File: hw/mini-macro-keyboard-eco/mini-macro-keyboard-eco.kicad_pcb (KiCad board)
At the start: 2 copper layers, 32 parts, among them J0 USB, J1 DEBUG_SWD, SW1 SW_Cherry_MX_1.00u_PCB, SW2 SW_Cherry_MX_1.00u_PCB, SW3 SW_Cherry_MX_1.00u_PCB, SW5 LAYOUT, SW6 BACKLIGHT, U1 USBLC6-2SC6, U2 XC6206P322MR, U3 STM32F070F6P6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

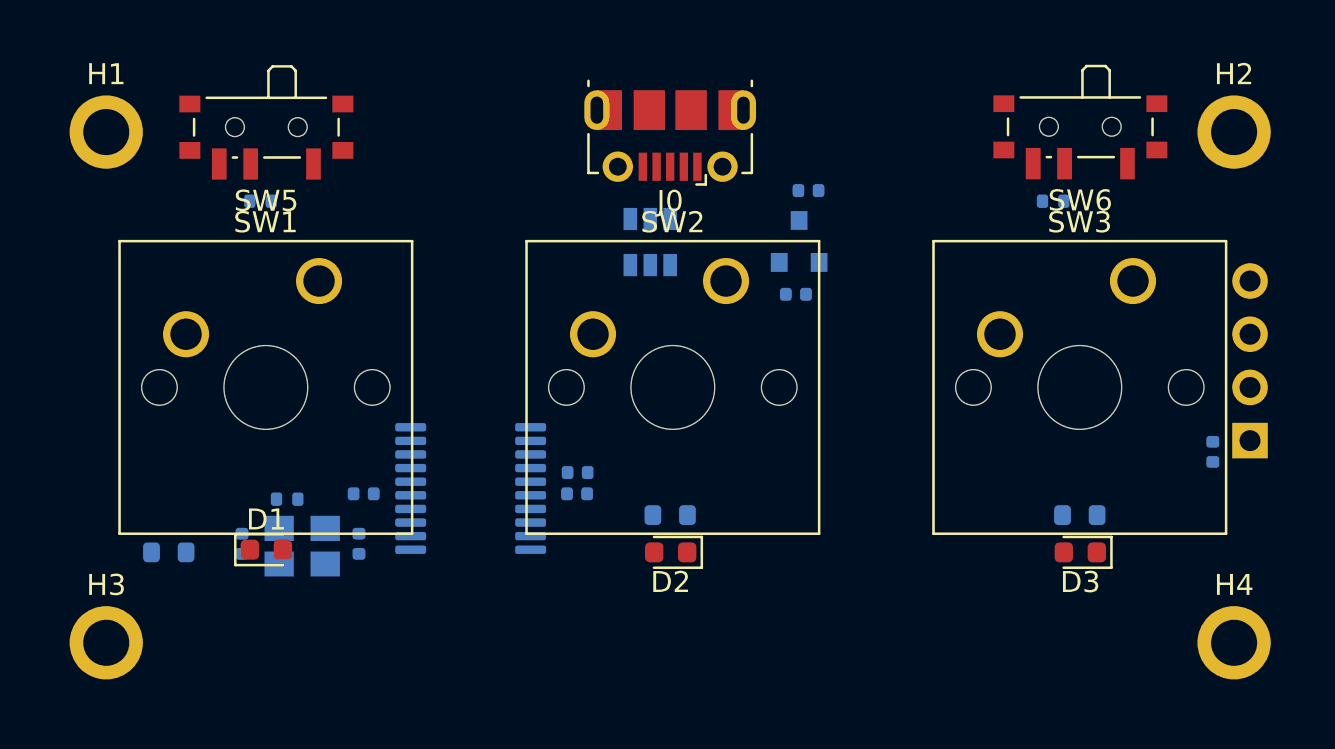
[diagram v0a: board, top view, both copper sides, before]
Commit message: feat(hw): improve layout
Signed-off-by: Ivan Kovalenko <s1ckretbox@gmail.com>
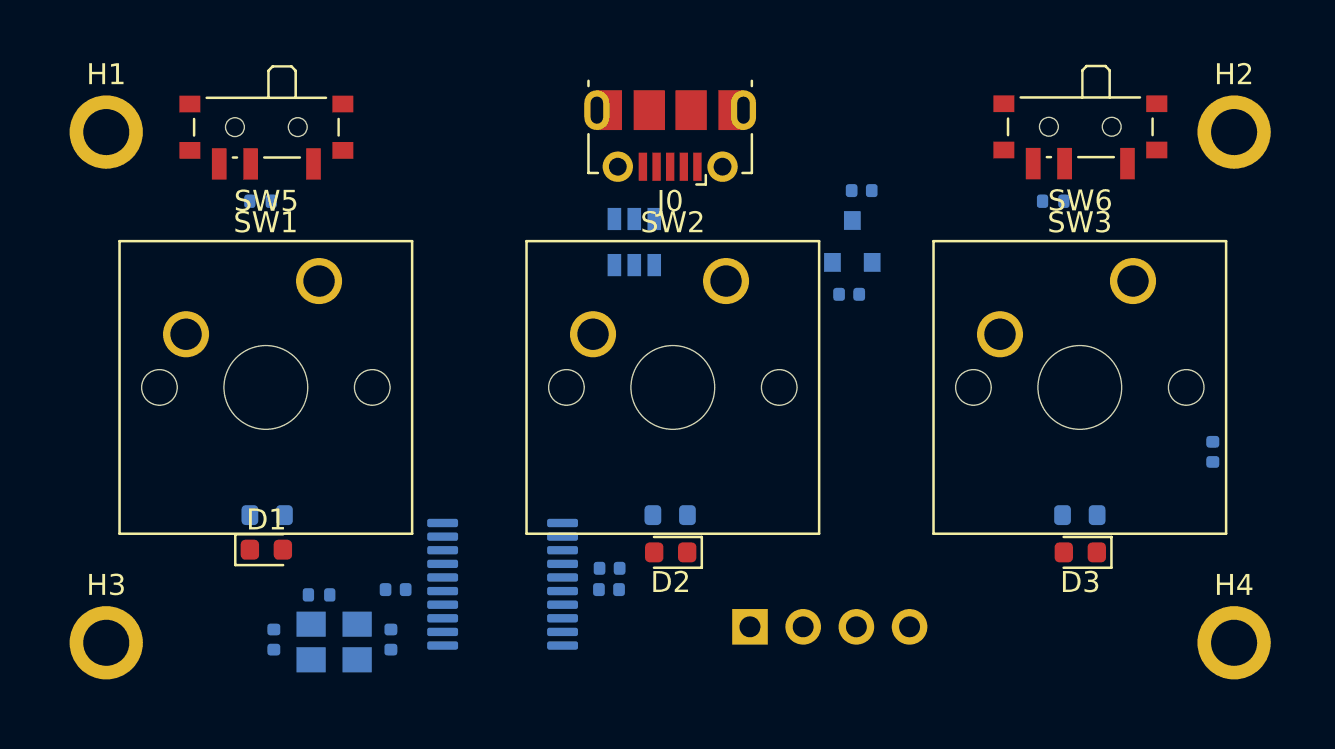
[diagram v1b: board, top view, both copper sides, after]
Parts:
- moved J1 25.5 mm to (147.1, 111.8), turned to 270 degrees
- moved R1 5.02 mm to (124.0, 106.4), turned to 0 degrees
- moved C0 4.82 mm to (129.9, 112.4)
- moved C1 4.82 mm to (124.3, 112.4)
- moved C2 4.82 mm to (140.3, 110.0)
- moved C3 4.82 mm to (130.1, 110.0)
- moved R0 4.82 mm to (126.5, 110.2)
- moved Y1 4.82 mm to (127.2, 112.5)
- moved C4 4.82 mm to (140.4, 109.0)
- moved U3 4.82 mm to (135.3, 109.7)
- moved C5 2.54 mm to (152.4, 90.9)
- moved C6 2.54 mm to (151.8, 95.9)
- moved U2 2.54 mm to (152.0, 93.4)
- moved U1 0.76 mm to (141.5, 93.4)
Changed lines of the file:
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@@
   )
   (module Capacitor_SMD:C_0402_1005Metric (layer B.Cu)
-    (at 138.811 105.41)
+    (at 140.335 109.982)
     (descr "Capacitor SMD 0402 (1005 Metric), square (rectangular) end terminal, IPC_7351 nominal, (Body size source: IPC-SM-782 page 76, https://www.pcb-3d.com/wordpress/wp-content/uploads/ipc-sm-782a_amendment_1_and_2.pdf), generated with kicad-footprint-generator")
     (tags capacitor)
@@
   )
   (module Capacitor_SMD:C_0402_1005Metric (layer B.Cu)
-    (at 128.623 105.41 180)
+    (at 130.147 109.982 180)
     (descr "Capacitor SMD 0402 (1005 Metric), square (rectangular) end terminal, IPC_7351 nominal, (Body size source: IPC-SM-782 page 76, https://www.pcb-3d.com/wordpress/wp-content/uploads/ipc-sm-782a_amendment_1_and_2.pdf), generated with kicad-footprint-generator")
     (tags capacitor)
@@
   )
   (module Capacitor_SMD:C_0402_1005Metric (layer B.Cu)
-    (at 138.839 104.394)
+    (at 140.363 108.966)
     (descr "Capacitor SMD 0402 (1005 Metric), square (rectangular) end terminal, IPC_7351 nominal, (Body size source: IPC-SM-782 page 76, https://www.pcb-3d.com/wordpress/wp-content/uploads/ipc-sm-782a_amendment_1_and_2.pdf), generated with kicad-footprint-generator")
     (tags capacitor)
@@
   )
   (module Capacitor_SMD:C_0402_1005Metric (layer B.Cu)
-    (at 122.809 107.795 90)
+    (at 124.333 112.367 90)
     (descr "Capacitor SMD 0402 (1005 Metric), square (rectangular) end terminal, IPC_7351 nominal, (Body size source: IPC-SM-782 page 76, https://www.pcb-3d.com/wordpress/wp-content/uploads/ipc-sm-782a_amendment_1_and_2.pdf), generated with kicad-footprint-generator")
     (tags capacitor)
@@
   )
   (module Capacitor_SMD:C_0402_1005Metric (layer B.Cu)
-    (at 128.397 107.795 270)
+    (at 129.921 112.367 270)
     (descr "Capacitor SMD 0402 (1005 Metric), square (rectangular) end terminal, IPC_7351 nominal, (Body size source: IPC-SM-782 page 76, https://www.pcb-3d.com/wordpress/wp-content/uploads/ipc-sm-782a_amendment_1_and_2.pdf), generated with kicad-footprint-generator")
     (tags capacitor)
@@
   )
   (module Capacitor_SMD:C_0402_1005Metric (layer B.Cu)
-    (at 149.86 90.932)
+    (at 152.4 90.932)
     (descr "Capacitor SMD 0402 (1005 Metric), square (rectangular) end terminal, IPC_7351 nominal, (Body size source: IPC-SM-782 page 76, https://www.pcb-3d.com/wordpress/wp-content/uploads/ipc-sm-782a_amendment_1_and_2.pdf), generated with kicad-footprint-generator")
     (tags capacitor)
@@
   )
   (module Capacitor_SMD:C_0402_1005Metric (layer B.Cu)
-    (at 149.2605 95.885)
+    (at 151.8005 95.885)
     (descr "Capacitor SMD 0402 (1005 Metric), square (rectangular) end terminal, IPC_7351 nominal, (Body size source: IPC-SM-782 page 76, https://www.pcb-3d.com/wordpress/wp-content/uploads/ipc-sm-782a_amendment_1_and_2.pdf), generated with kicad-footprint-generator")
     (tags capacitor)
@@
   )
   (module Connector_PinHeader_2.54mm:PinHeader_1x04_P2.54mm_Horizontal (layer B.Cu)
-    (at 170.942 102.87)
+    (at 147.066 111.76 270)
     (descr "Through hole angled pin header, 1x04, 2.54mm pitch, 6mm pin length, single row")
     (tags "Through hole angled pin header THT 1x04 2.54mm single row")
-    (fp_text reference J1 (at 4.385 2.27) (layer B.SilkS)
-      (effects (font (size 1 1) (thickness 0.15)) (justify mirror))
-    )
-    (fp_text value DEBUG_SWD (at 4.385 -9.89) (layer B.Fab)
+    (fp_text reference J1 (at 4.385 2.27 90) (layer B.SilkS)
+      (effects (font (size 1 1) (thickness 0.15)) (justify mirror))
+    )
+    (fp_text value DEBUG_SWD (at 4.385 -9.89 90) (layer B.Fab)
       (effects (font (size 1 1) (thickness 0.15)) (justify mirror))
     )
@@
     (fp_line (start 4.04 1.27) (end 4.04 -8.89) (layer B.Fab) (width 0.1))
     (fp_line (start 2.135 1.27) (end 4.04 1.27) (layer B.Fab) (width 0.1))
-    (fp_text user %R (at 2.77 -3.81 -90) (layer B.Fab)
-      (effects (font (size 1 1) (thickness 0.15)) (justify mirror))
-    )
-    (pad 1 thru_hole rect (at 0 0) (size 1.7 1.7) (drill 1) (layers *.Cu *.Mask)
+    (fp_text user %R (at 2.77 -3.81 180) (layer B.Fab)
+      (effects (font (size 1 1) (thickness 0.15)) (justify mirror))
+    )
+    (pad 1 thru_hole rect (at 0 0 270) (size 1.7 1.7) (drill 1) (layers *.Cu *.Mask)
       (net 2 +3V3))
-    (pad 2 thru_hole oval (at 0 -2.54) (size 1.7 1.7) (drill 1) (layers *.Cu *.Mask)
+    (pad 2 thru_hole oval (at 0 -2.54 270) (size 1.7 1.7) (drill 1) (layers *.Cu *.Mask)
       (net 17 SWDIO))
-    (pad 3 thru_hole oval (at 0 -5.08) (size 1.7 1.7) (drill 1) (layers *.Cu *.Mask)
+    (pad 3 thru_hole oval (at 0 -5.08 270) (size 1.7 1.7) (drill 1) (layers *.Cu *.Mask)
       (net 18 SWCLK))
-    (pad 4 thru_hole oval (at 0 -7.62) (size 1.7 1.7) (drill 1) (layers *.Cu *.Mask)
+    (pad 4 thru_hole oval (at 0 -7.62 270) (size 1.7 1.7) (drill 1) (layers *.Cu *.Mask)
       (net 1 GND))
     (model ${KISYS3DMOD}/Connector_PinHeader_2.54mm.3dshapes/PinHeader_1x04_P2.54mm_Horizontal.wrl
@@
   )
   (module Resistor_SMD:R_0402_1005Metric (layer B.Cu)
-    (at 124.97 105.664 180)
+    (at 126.494 110.236 180)
     (descr "Resistor SMD 0402 (1005 Metric), square (rectangular) end terminal, IPC_7351 nominal, (Body size source: IPC-SM-782 page 72, https://www.pcb-3d.com/wordpress/wp-content/uploads/ipc-sm-782a_amendment_1_and_2.pdf), generated with kicad-footprint-generator")
     (tags resistor)
@@
   )
   (module Resistor_SMD:R_0603_1608Metric (layer B.Cu)
-    (at 119.317 108.204 180)
+    (at 124.015 106.426)
     (descr "Resistor SMD 0603 (1608 Metric), square (rectangular) end terminal, IPC_7351 nominal, (Body size source: IPC-SM-782 page 72, https://www.pcb-3d.com/wordpress/wp-content/uploads/ipc-sm-782a_amendment_1_and_2.pdf), generated with kicad-footprint-generator")
     (tags resistor)
@@
       (effects (font (size 0.4 0.4) (thickness 0.06)) (justify mirror))
     )
-    (pad 1 smd roundrect (at -0.825 0 180) (size 0.8 0.95) (layers B.Cu B.Paste B.Mask) (roundrect_rratio 0.25)
+    (pad 1 smd roundrect (at -0.825 0) (size 0.8 0.95) (layers B.Cu B.Paste B.Mask) (roundrect_rratio 0.25)
       (net 8 "Net-(D1-Pad1)"))
-    (pad 2 smd roundrect (at 0.825 0 180) (size 0.8 0.95) (layers B.Cu B.Paste B.Mask) (roundrect_rratio 0.25)
+    (pad 2 smd roundrect (at 0.825 0) (size 0.8 0.95) (layers B.Cu B.Paste B.Mask) (roundrect_rratio 0.25)
       (net 1 GND))
     (model ${KISYS3DMOD}/Resistor_SMD.3dshapes/R_0603_1608Metric.wrl
@@
   )
   (module Package_TO_SOT_SMD:SOT-23-6 (layer B.Cu)
-    (at 142.306 93.388 90)
+    (at 141.544 93.388 90)
     (descr "6-pin SOT-23 package")
     (tags SOT-23-6)
@@
   )
   (module Package_TO_SOT_SMD:SOT-23 (layer B.Cu)
-    (at 149.413 93.361 90)
+    (at 151.953 93.361 90)
     (descr "SOT-23, Standard")
     (tags SOT-23)
@@
   )
   (module Package_SO:TSSOP-20_4.4x6.5mm_P0.65mm (layer B.Cu)
-    (at 133.731 105.156)
+    (at 135.255 109.728)
     (descr "TSSOP, 20 Pin (JEDEC MO-153 Var AC https://www.jedec.org/document_search?search_api_views_fulltext=MO-153), generated with kicad-footprint-generator ipc_gullwing_generator.py")
     (tags "TSSOP SO")
@@
   )
   (module Crystal:Crystal_SMD_3225-4Pin_3.2x2.5mm (layer B.Cu)
-    (at 125.687 107.911 180)
+    (at 127.211 112.483 180)
     (descr "SMD Crystal SERIES SMD3225/4 http://www.txccrystal.com/images/pdf/7m-accuracy.pdf, 3.2x2.5mm^2 package")
     (tags "SMD SMT crystal")

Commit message: feat(hw): add edges
Signed-off-by: Ivan Kovalenko <s1ckretbox@gmail.com>
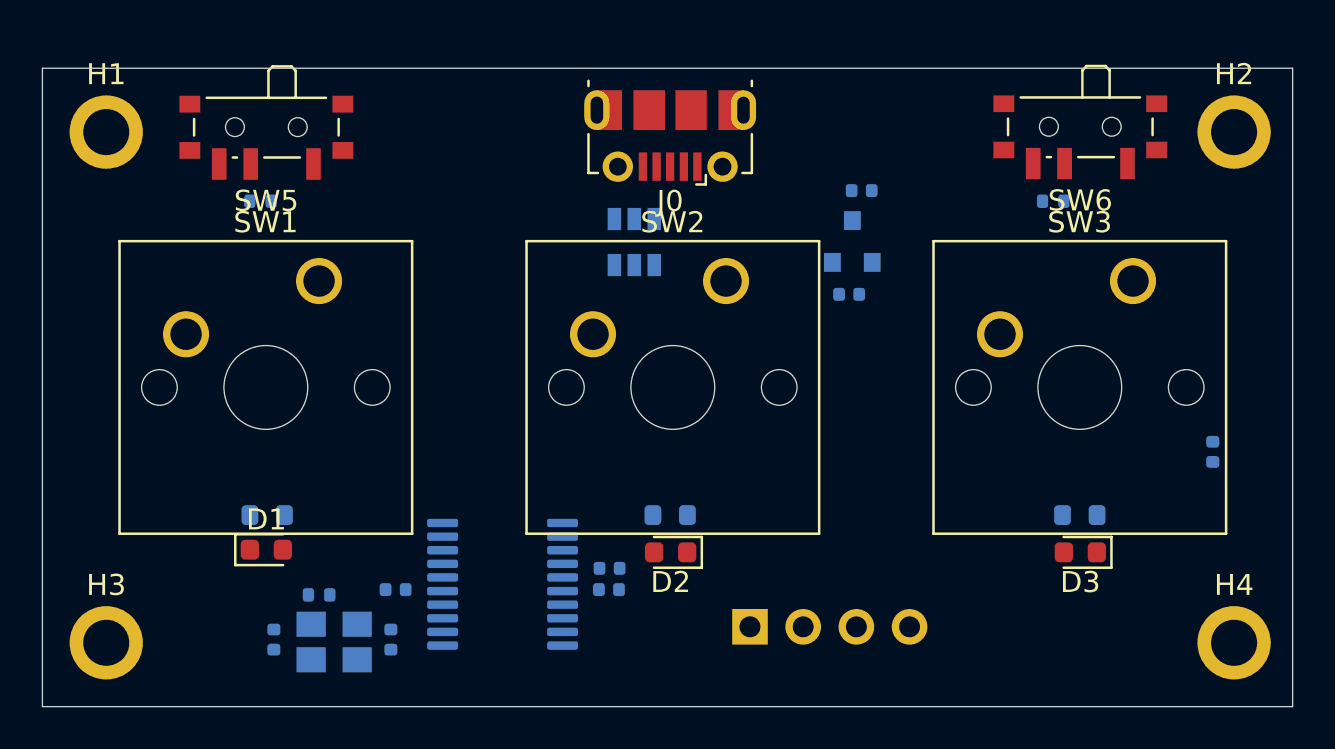
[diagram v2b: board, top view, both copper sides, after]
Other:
- board outline added: 59.7 x 30.5 mm
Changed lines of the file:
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@@
   (general
     (thickness 1.6)
-    (drawings 0)
+    (drawings 6)
     (tracks 0)
     (zones 0)
@@
     )
   )
+  (gr_line (start 113.284 85.09) (end 116.332 85.09) (layer Edge.Cuts) (width 0.05))
+  (gr_line (start 113.284 115.57) (end 113.284 85.09) (layer Edge.Cuts) (width 0.05))
+  (gr_line (start 172.974 115.57) (end 113.284 115.57) (layer Edge.Cuts) (width 0.05))
+  (gr_line (start 172.974 85.09) (end 172.974 115.57) (layer Edge.Cuts) (width 0.05))
+  (gr_line (start 170.18 85.09) (end 172.974 85.09) (layer Edge.Cuts) (width 0.05))
+  (gr_line (start 116.332 85.09) (end 170.18 85.09) (layer Edge.Cuts) (width 0.05))
 )

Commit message: feat(hw): move usb-b to the back layer
Signed-off-by: Ivan Kovalenko <s1ckretbox@gmail.com>
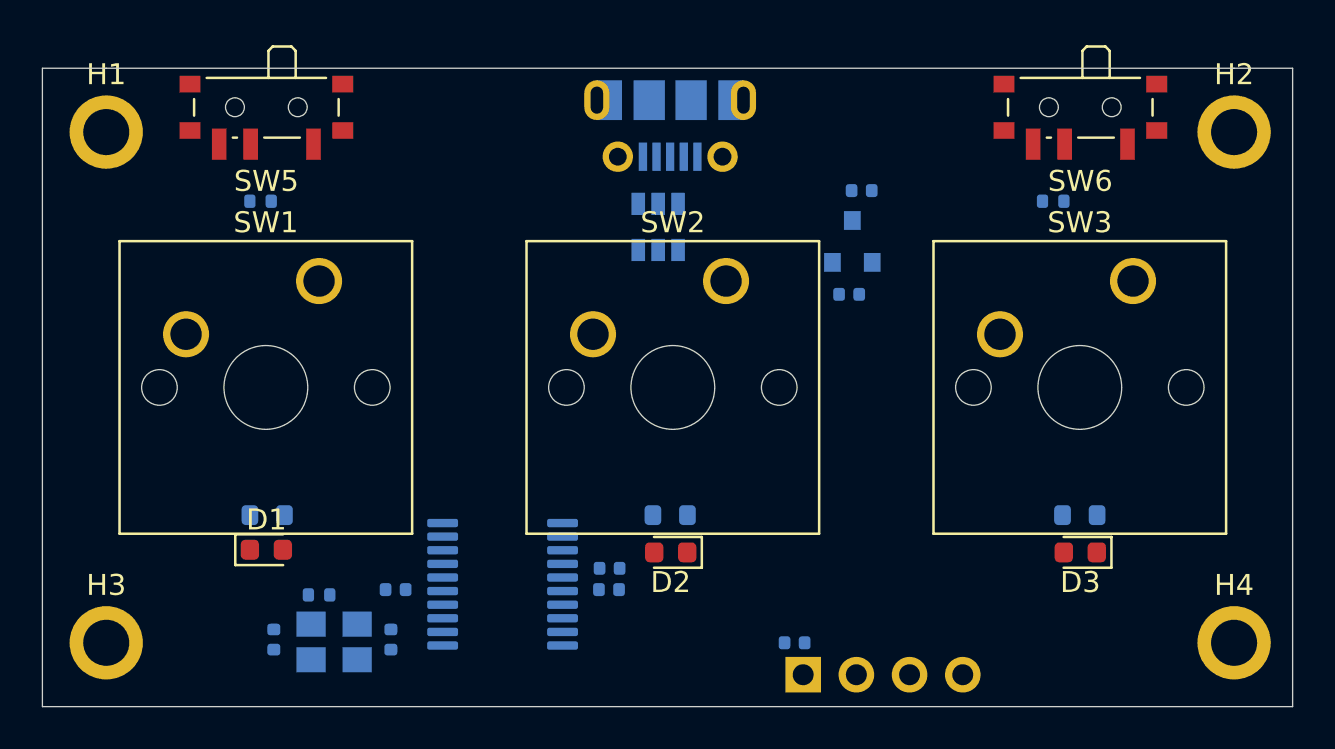
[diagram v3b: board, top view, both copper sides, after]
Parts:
- J0: moved to B.Cu
- moved C7 21.9 mm to (149.2, 112.5), turned to 180 degrees
- moved J1 3.42 mm to (149.6, 114.0)
- moved U1 1.35 mm to (142.7, 92.7), turned to 270 degrees
- moved SW5 0.95 mm to (124.0, 87.3)
- moved SW6 0.93 mm to (162.8, 87.3)
- moved J0 0.48 mm to (143.3, 87.9), turned to 0 degrees

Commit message: feat(hw): add rooting
Signed-off-by: Ivan Kovalenko <s1ckretbox@gmail.com>
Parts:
- moved R5 39.2 mm to (162.9, 91.5), turned to 0 degrees
- moved SW6 39.0 mm to (123.8, 87.1)
- moved SW5 39.0 mm to (162.9, 87.1)
- moved R6 36.8 mm to (124.8, 91.6), turned to 180 degrees
- moved C7 2.60 mm to (146.6, 112.9)
- moved R0 1.48 mm to (127.9, 110.7)
- moved R3 1.33 mm to (162.8, 105.1)
- moved R2 1.33 mm to (143.3, 105.1)
- moved R1 1.33 mm to (124.0, 105.1)
- moved J1 1.14 mm to (149.6, 112.9)
- moved U1 0.93 mm to (142.6, 93.6)
- moved C0 0.52 mm to (130.0, 112.9)
- moved C1 0.52 mm to (124.5, 112.9)
- moved Y1 0.52 mm to (127.3, 113.0)
- moved H1 0.51 mm to (116.8, 88.1)
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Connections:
- U1 pad 1: USB_CONN_D+ -> USB_CONN_D-
- U1 pad 3: USB_CONN_D- -> USB_CONN_D+
- U1 pad 4: USB_D- -> USB_D+
- U1 pad 6: USB_D+ -> USB_D-
- U3 pad 11: SW_1 -> SW_3
- U3 pad 13: SW_3 -> SW_1
- U3 pad 6: LED_1 -> LED_3
- U3 pad 9: LED_3 -> LED_1
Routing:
- net SW_LAYOUT: track 0.00 -> 39.1 mm, vias 0 -> 2
- net GND: track 0.00 -> 30.6 mm, vias 0 -> 10
- net LED_3: track 0.00 -> 30.2 mm, vias 0 -> 1
- net SW_1: track 0.00 -> 26.0 mm, vias 0 -> 1
- net SW_3: track 0.00 -> 25.2 mm, vias 0 -> 1
- net +5V: track 0.00 -> 23.1 mm, vias 0 -> 3
- net USB_D+: track 0.00 -> 22.9 mm
- net USB_D-: track 0.00 -> 22.1 mm
- net SW_BACKLIGHT: track 0.00 -> 20.1 mm
- net +3V3: track 0.00 -> 18.2 mm, vias 0 -> 4
- net SWCLK: track 0.00 -> 17.7 mm
- net SWDIO: track 0.00 -> 15.5 mm
- net SW_2: track 0.00 -> 13.2 mm, vias 0 -> 1
- net LED_2: track 0.00 -> 10.3 mm, vias 0 -> 1
- net LED_1: track 0.00 -> 8.02 mm, vias 0 -> 1
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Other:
- board size 59.7 x 30.5 mm -> 59.2 x 30.5 mm
